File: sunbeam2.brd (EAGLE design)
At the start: 120 x 95 mm, 276 parts, among them IC10 LM1117IMPX-3.3, IC2 A4983, IC3 A4983, IC4 A4983, IC5 A4983, IC6 A4983, IC7 FT232RLSSOP, IC8 LM2675, IC9 LMV358MMX, Q1 BC857ALT1SMD, Q2 IRLHM630TR2PBF, Q3 IRLHM630TR2PBF, Q4 IRLHM630TR2PBF, T1 IRLML2246TRPBF, U2 USD-SOCKETNEW

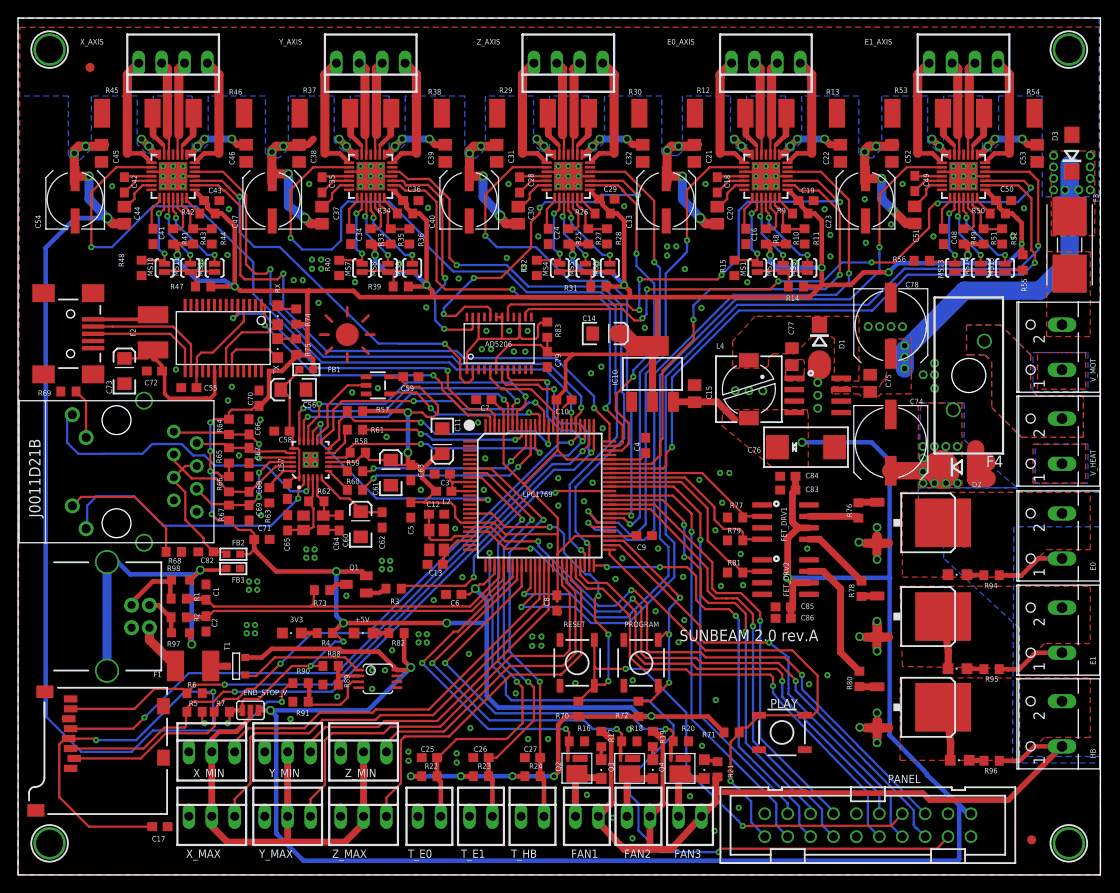
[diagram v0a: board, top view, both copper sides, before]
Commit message: added paste layer for tranzistors
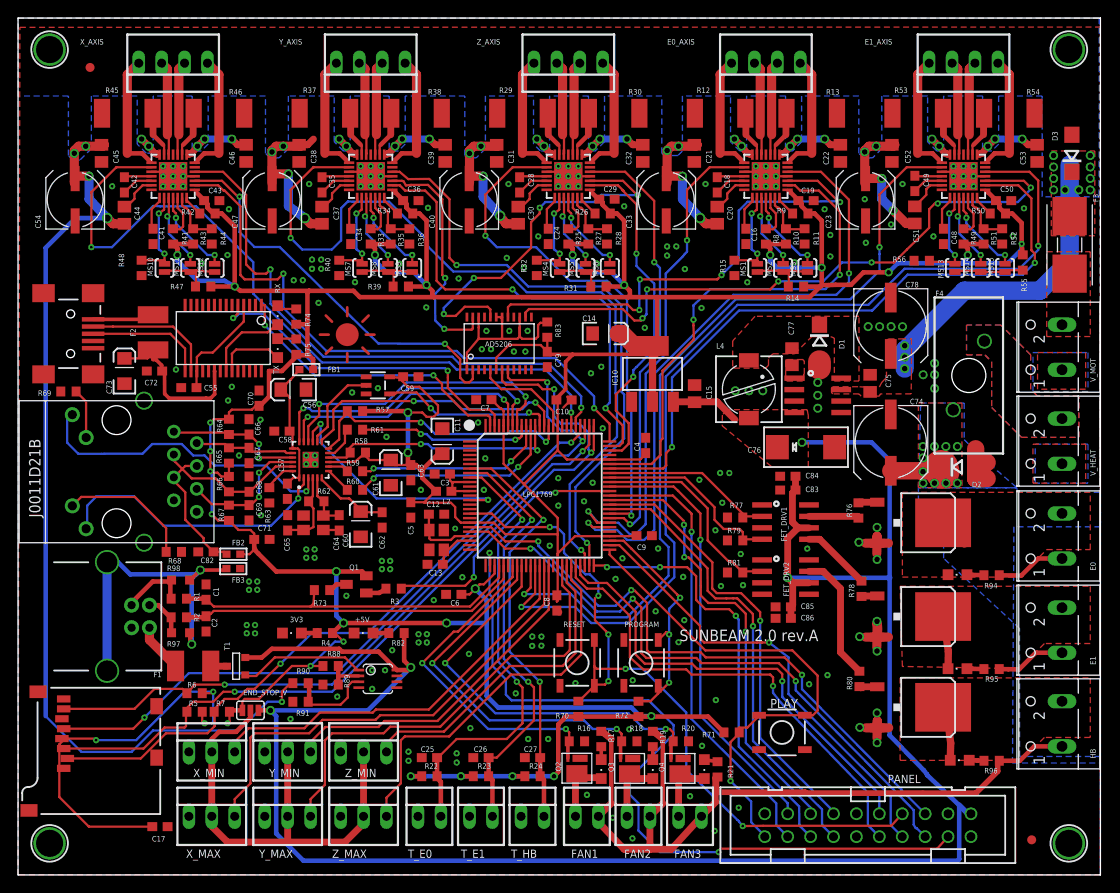
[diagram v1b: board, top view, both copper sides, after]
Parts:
- moved U2 0.76 mm to (15.8, 20.8)
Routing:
- net V_EXTR: track 113.3 -> 105.7 mm
- net SD_SCK: track 86.1 -> 86.9 mm
- net SD_MOSI: track 93.1 -> 93.9 mm
- net SD_MISO: track 72.2 -> 72.9 mm
- net SD_CS: track 73.0 -> 73.7 mm
- net ENET_RX_ER: track 28.2 -> 27.5 mm
- net +3V3: track 620.0 -> 620.7 mm
- net ENET_MDIO: track 31.1 -> 30.6 mm
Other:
- board text added: "C:/Documents and Settings/abdel/Moje dokumenty/Moje obrazy/logo2.bmp"
